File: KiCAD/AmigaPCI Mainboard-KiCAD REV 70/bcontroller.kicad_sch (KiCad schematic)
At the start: 36 parts, among them CN409 SPI, J211 FLASH_DIS, J212 ROM WAIT, J409_TP0 U409_TP, J900 AUTOBOOT, U214 74LVC244, U409 ICE40HX4K-TQ144, U409F1 W25X20CLSN

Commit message: Add JLCPCB part numbers and fix 74LVC244 footprints.
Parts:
- C254, C420, C421, C429, C430, C431, C432, C433, C434, C435, C436, C438, C440: LCSC (none) -> C14663
- C437, C439: LCSC (none) -> C96446
- CN409: LCSC (none) -> C37208
- J211, J409_TP0, J900: LCSC (none) -> C124375
- J212: LCSC (none) -> C66690
- R217, R220, R270, R272, R273, R274, R275: LCSC (none) -> C23345
- R286, R287: LCSC (none) -> C21190
- R400, R401: LCSC (none) -> C22775
- R402, R403: LCSC (none) -> C25804
- U214: footprint Package_SO:SSOP-20_4.4x6.5mm_P0.65mm -> Package_SO:TSSOP-20_4.4x6.5mm_P0.65mm; LCSC (none) -> C7668
- U409: LCSC (none) -> C1521989
- U409F1: LCSC (none) -> C34591

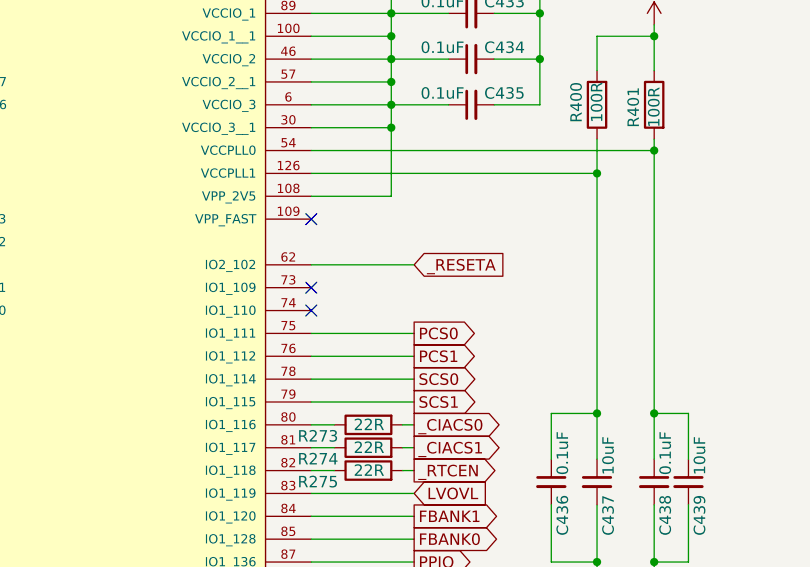
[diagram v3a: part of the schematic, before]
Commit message: Updates to revision 7 board.
Change U810 to 74LVC245 buffers
Add CDAC to U712
Add address latch to CIAs
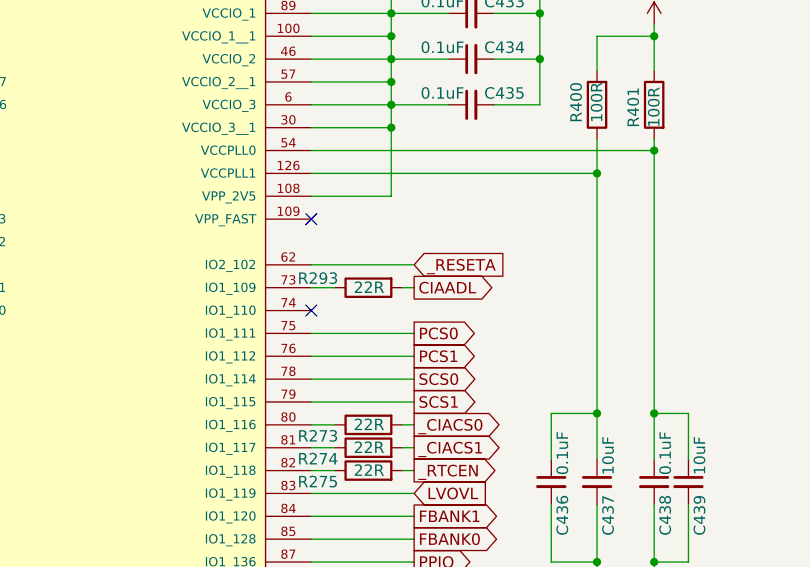
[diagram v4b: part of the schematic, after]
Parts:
- added R293: 22R, Resistor_SMD:R_0603_1608Metric, symbol Device:R
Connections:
- net at U409.73 (IO1_109): now also R293.1
- new net CIAADL: R293.2
- no-connect marks 8 -> 7
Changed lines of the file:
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@@
 	(title_block
 		(title "AMIGA PCI")
-		(date "2026-04-27")
+		(date "2026-06-06")
 		(rev "7.0")
 	)
@@
 	)
 	(no_connect
-		(at 207.01 93.98)
-	)
-	(no_connect
 		(at 207.01 86.36)
 	)
@@
 	(wire
 		(pts
+			(xy 217.17 93.98) (xy 218.44 93.98)
+		)
+		(stroke
+			(width 0)
+			(type default)
+		)
+	)
+	(wire
+		(pts
 			(xy 215.9 193.04) (xy 207.01 193.04)
 		)
@@
 	(wire
 		(pts
+			(xy 207.01 93.98) (xy 209.55 93.98)
+		)
+		(stroke
+			(width 0)
+			(type default)
+		)
+	)
+	(wire
+		(pts
 			(xy 147.32 160.02) (xy 156.21 160.02)
 		)
@@
 		)
 	)
+	(global_label "CIAADL"
+		(shape output)
+		(at 218.44 93.98 0)
+		(fields_autoplaced yes)
+		(effects
+			(font
+				(size 1.27 1.27)
+			)
+			(justify left)
+		)
+		(property "Intersheetrefs" "${INTERSHEET_REFS}"
+			(at 227.7753 93.98 0)
+			(effects
+				(font
+					(size 1.27 1.27)
+				)
+				(justify left)
+			)
+		)
+	)
 	(global_label "U110_SDI"
 		(shape output)
@@
 					(unit 1)
 				)
+			)
+		)
+	)
+	(symbol
+		(lib_id "Device:R")
+		(at 213.36 93.98 90)
+		(mirror x)
+		(unit 1)
+		(exclude_from_sim no)
+		(in_bom yes)
+		(on_board yes)
+		(dnp no)
+		(property "Reference" "R293"
+			(at 205.486 92.964 90)
+			(effects
+				(font
+					(size 1.27 1.27)
+				)
+				(justify right)
+			)
+		)
+		(property "Value" "22R"
+			(at 215.138 93.98 90)
+			(effects
+				(font
+					(size 1.27 1.27)
+				)
+				(justify left)
+			)
+		)
+		(property "Footprint" "Resistor_SMD:R_0603_1608Metric"
+			(at 213.36 92.202 90)
+			(effects
+				(font
+					(size 1.27 1.27)
+				)
+				(hide yes)
+			)
+		)
+		(property "Datasheet" "~"
+			(at 213.36 93.98 0)
+			(effects
+				(font
+					(size 1.27 1.27)
+				)
+				(hide yes)
+			)
+		)
+		(property "Description" ""
+			(at 213.36 93.98 0)
+			(effects
+				(font
+					(size 1.27 1.27)
+				)
+				(hide yes)
+			)
+		)
+		(property "LCSC" "C23345"
+			(at 213.36 93.98 0)
+			(effects
+				(font
+					(size 1.27 1.27)
+				)
+				(hide yes)
+			)
+		)
+		(pin "1"
+		)
+		(pin "2"
+		)
+		(instances
+			(project "AmigaPCI Mainboard"
+				(path "/72453515-27fe-4336-91f3-e3c8054f7767/62a07d55-3759-49a3-8a3f-631cb4902a24"
+					(reference "R293")
+					(unit 1)
+				)
